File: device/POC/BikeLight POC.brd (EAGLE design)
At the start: 68.6 x 53.3 mm, 3 parts

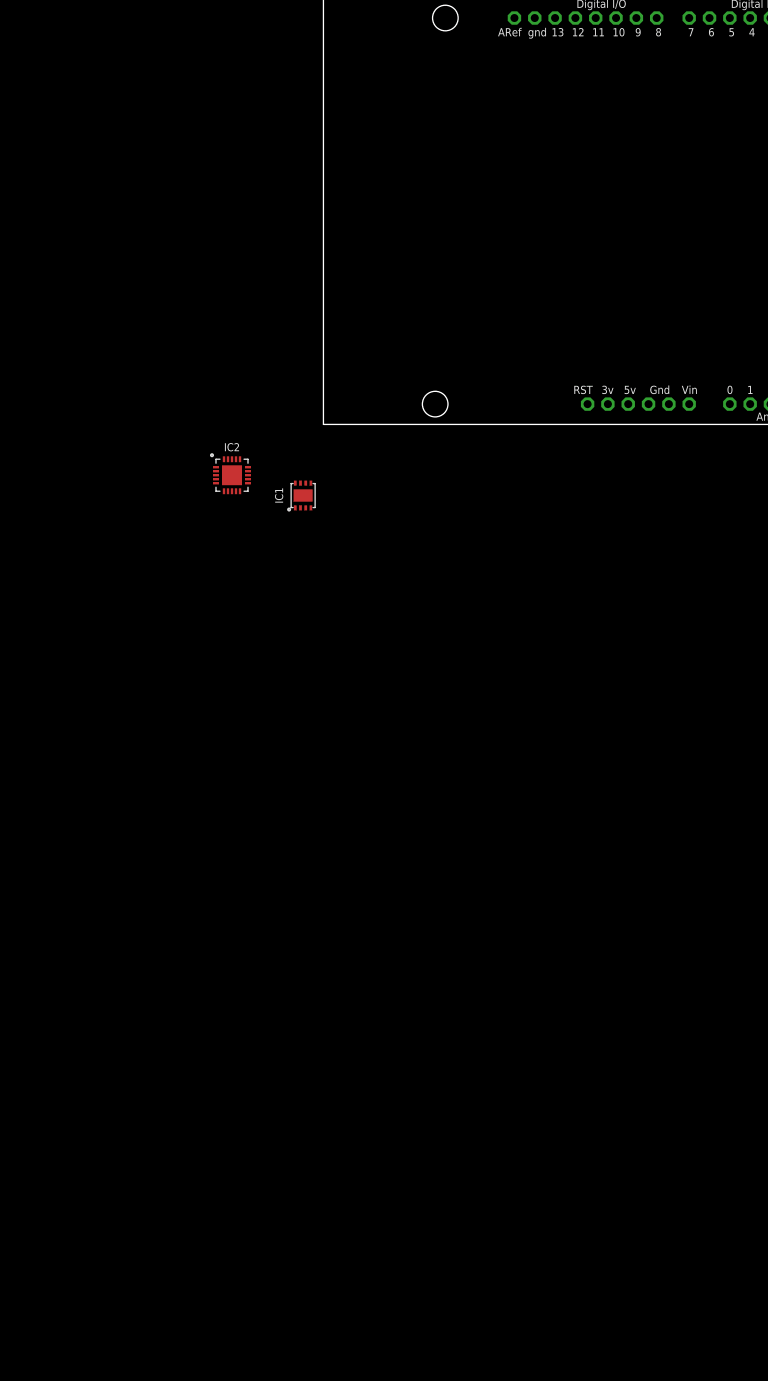
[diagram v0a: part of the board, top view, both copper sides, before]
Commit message: - added SD card with level shifter, FRAM module
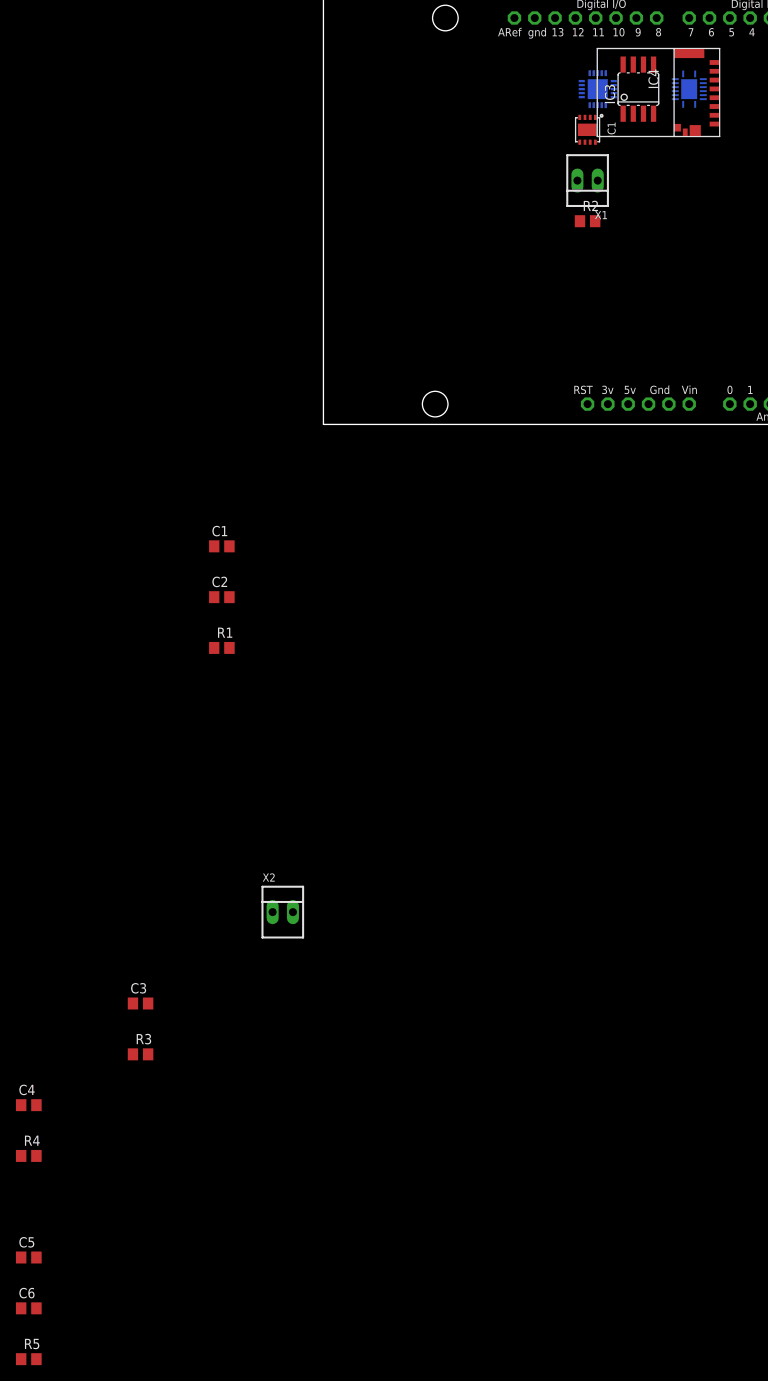
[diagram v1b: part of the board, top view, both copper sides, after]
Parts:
- added C1, C2, C3, C4, C5, C6: 0.1μF, rcl:C0805
- added IC3: FM25W256-SOIC, FM25W256 FERAM:SOIC08
- added IC4: MICROSD_SPI_MODE, Molex SD-47309 SD Card Slot:MICRO_SD_CONNECTOR
- added IC5: (no value), TXB0106 - Logic Level Translator:VQFN16
- added R1, R3, R4, R5: 10k, rcl:R0805
- added R2: 120, rcl:R0805
- added X1, X2: 22-23-2021, con-molex:22-23-2021
- moved IC2 66.5 mm to (34.3, 41.9), flipped to the bottom, turned to 180 degrees
- moved IC1 57.9 mm to (33.0, 36.8), turned to 180 degrees
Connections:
- removed net N$4: IC2.SI
- removed net N$5: IC2.SCK
- removed net N$6: IC2.!CS!
- removed net N$8: IC2.TXCAN
- removed net N$9: IC2.RXCAN
- removed net SPI_SS: U$1.D10
- removed net VCC: IC1.VDD
- removed net VDD: IC2.VDD
- new net 3V3: C4.1, C5.1, IC4.VDD, IC5.VCCA, R4.2
- new net 5V0: C1.1, C2.1, C3.1, C6.1, IC1.VDD, IC2.VDD, IC3.!HOLD!, IC3.!WP!, IC3.VCC, IC5.VCCB, R1.1, R3.2
- new net CANH: IC1.CANH, R2.2, X1.1
- new net CANL: IC1.CANL, R2.1, X1.2
- new net OE: IC5.OE, R5.2, U$1.D7
- new net RXCAN: IC1.RXD, IC2.RXCAN
- new net SD_CARD_DETECT: IC5.B6, U$1.D6
- new net SD_CARD_DETECT_3V3: IC4.DET, IC5.A6
- new net SPI_MISO_3V3: IC4.DAT0, IC5.A2
- new net SPI_MOSI_3V3: IC4.CMD, IC5.A4
- new net SPI_SCK_3V3: IC4.CLK, IC5.A3
- new net SPI_SS_FRAM: IC3.!CS!, R3.1, U$1.D9
- new net SPI_SS_MCP2515: IC2.!CS!, R1.2, U$1.D10
- new net SPI_SS_SD-CARD: IC5.B5, U$1.D8
- new net SPI_SS_SD-CARD_3V3: IC4.CD/DAT3, IC5.A5, R4.1
- new net STBY: IC1.STBY, U$1.D5
- new net TXCAN: IC1.TXD, IC2.TXCAN
- net GND: now also C1.2, C2.2, C3.2, C4.2, C5.2, C6.2, IC3.GND, IC4.GND2, IC4.GND4, IC4.POL, IC4.VSS, IC5.GND, IC5.GND1, R5.1
- net N$3: now also IC2.OSC1; no longer IC2.SO
- net SPI_MISO: now also IC2.SO, IC3.SO, IC5.B2
- net SPI_MOSI: now also IC2.SI, IC3.SI, IC5.B4
- net SPI_SCK: now also IC2.SCK, IC3.SCK, IC5.B3

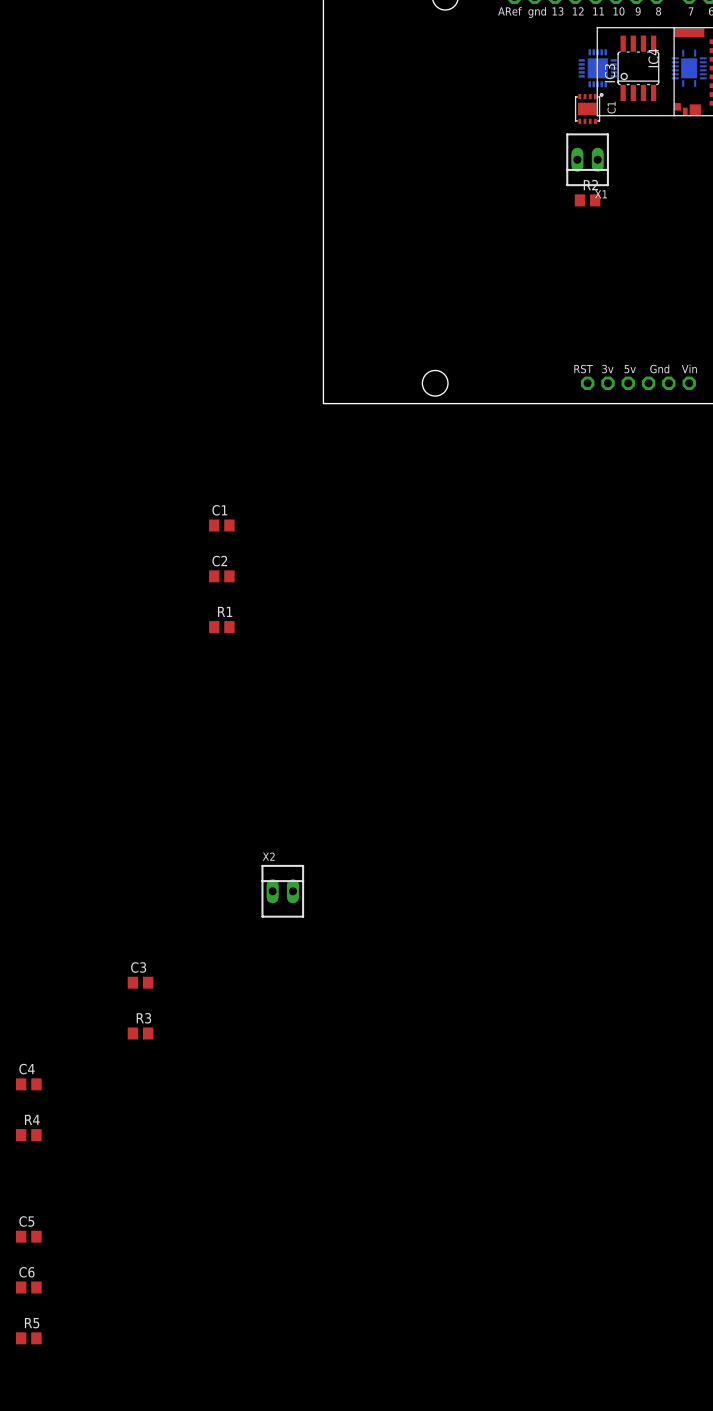
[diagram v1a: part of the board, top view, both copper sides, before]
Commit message: - added few passives to SD card, FRAM, logic level shifter, can hardware
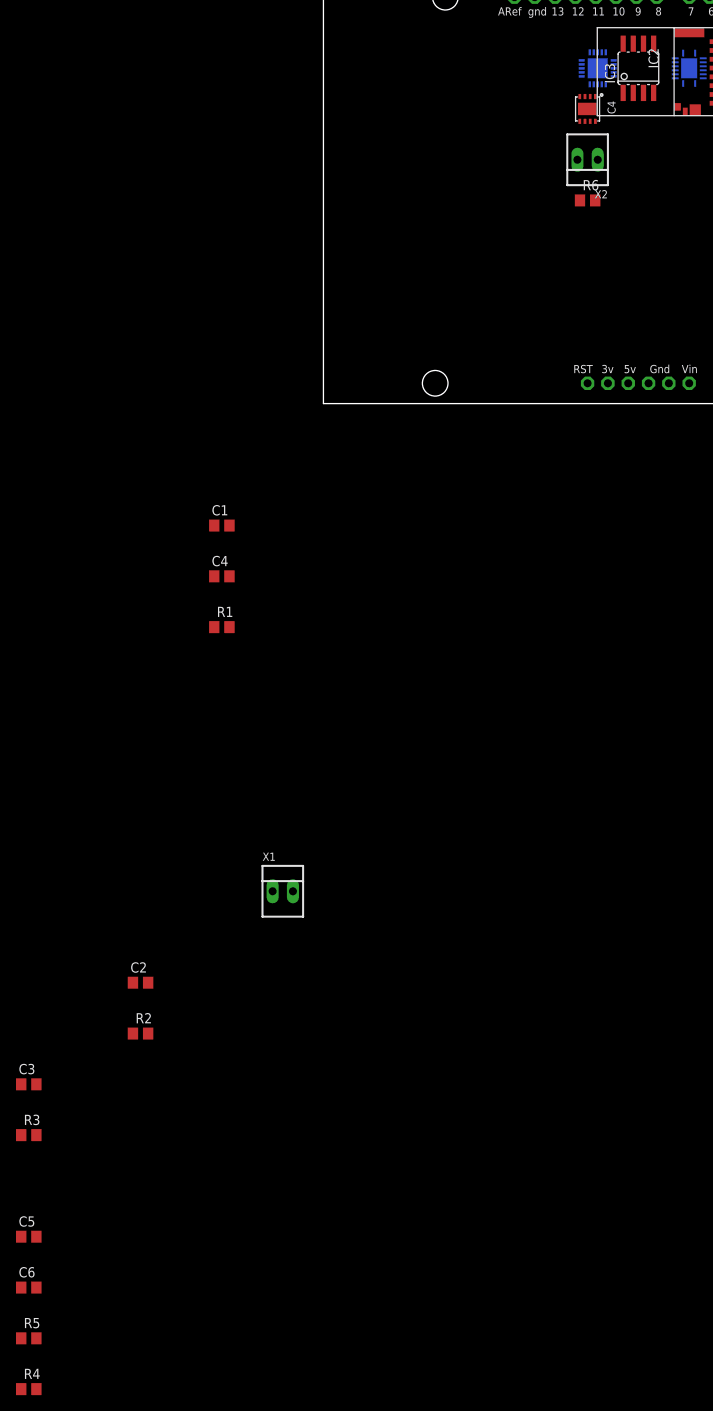
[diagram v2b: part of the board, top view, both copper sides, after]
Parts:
- added R6: 120, rcl:R0805
- BRD1: value ARDUINOUNO -> (none)
- IC1: device MCP2561-2 - High-Speed CAN Transceiver:DFN10 -> MCP2515-I-ML - Standalonce CAN Controller with SPI Interface:QFN20
- IC2: value (none) -> MICROSD_SPI_MODE; device MCP2515-I-ML - Standalonce CAN Controller with SPI Interface:QFN20 -> Molex SD-47309 SD Card Slot:MICRO_SD_CONNECTOR
- IC4: value MICROSD_SPI_MODE -> (none); device Molex SD-47309 SD Card Slot:MICRO_SD_CONNECTOR -> MCP2561-2 - High-Speed CAN Transceiver:DFN10
- R2: value 120 -> 10k
- moved R2 118.2 mm to (-22.9, -78.7)
- moved X1 99.1 mm to (-5.08, -61.0), turned to 0 degrees
- moved X2 99.1 mm to (33.0, 30.5), turned to 180 degrees
- moved C4 67.9 mm to (-12.7, -21.6)
- moved C2 51.8 mm to (-22.9, -72.4)
- moved R4 31.8 mm to (-36.8, -123.2)
- moved IC4 19.4 mm to (33.0, 36.8), turned to 180 degrees
- moved C3 18.9 mm to (-36.8, -85.1)
- moved R3 18.9 mm to (-36.8, -91.4)
- moved IC2 16.1 mm to (49.5, 47.0), flipped to the top, turned to 270 degrees
- moved IC1 5.24 mm to (34.3, 41.9), flipped to the bottom
- renumbered U$1 to BRD1
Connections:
- net 3V3: now also C3.1, IC2.VDD, R3.2; no longer C4.1, IC4.VDD, R4.2
- net 5V0: now also C4.1, IC4.VDD, R2.2, R4.1; no longer C3.1, IC2.VDD, R3.2
- net CANH: now also IC4.CANH, R6.2, X2.1; no longer IC1.CANH, R2.2, X1.1
- net CANL: now also IC4.CANL, R6.1, X2.2; no longer IC1.CANL, R2.1, X1.2
- net GND: now also IC1.GND1, IC1.GND6, IC2.GND2, IC2.GND4, IC2.POL, IC2.VSS, IC4.GND; no longer IC1.VSS, IC2.GND, IC2.GND1, IC2.GND6, IC4.GND2, IC4.GND4, IC4.POL
- net N$3: now also IC1.OSC1; no longer IC2.OSC1
- net N$7: now also IC1.!INT!; no longer IC2.!INT!
- net RXCAN: now also IC1.RXCAN, IC4.RXD; no longer IC1.RXD, IC2.RXCAN
- net SD_CARD_DETECT_3V3: now also IC2.DET; no longer IC4.DET
- net SPI_MISO: now also IC1.SO; no longer IC2.SO
- net SPI_MISO_3V3: now also IC2.DAT0; no longer IC4.DAT0
- net SPI_MOSI: now also IC1.SI; no longer IC2.SI
- net SPI_MOSI_3V3: now also IC2.CMD; no longer IC4.CMD
- net SPI_SCK: now also IC1.SCK; no longer IC2.SCK
- net SPI_SCK_3V3: now also IC2.CLK; no longer IC4.CLK
- net SPI_SS_FRAM: now also R2.1; no longer R3.1
- net SPI_SS_MCP2515: now also IC1.!CS!; no longer IC2.!CS!
- net SPI_SS_SD-CARD_3V3: now also IC2.CD/DAT3, R3.1; no longer IC4.CD/DAT3, R4.1
- net STBY: now also IC4.STBY, R4.2; no longer IC1.STBY
- net TXCAN: now also IC1.TXCAN, IC4.TXD; no longer IC1.TXD, IC2.TXCAN

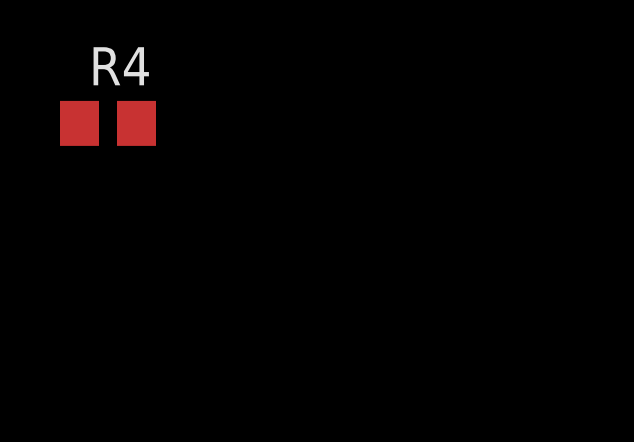
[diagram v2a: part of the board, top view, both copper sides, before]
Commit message: - added 8mhz oscillator to mcp2515
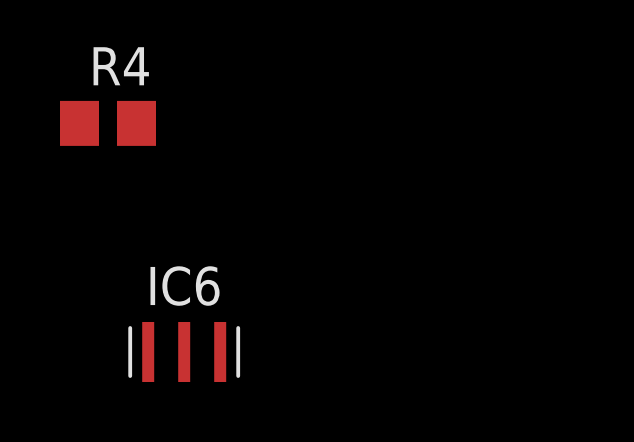
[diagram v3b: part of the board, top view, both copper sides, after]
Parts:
- added IC6: (no value), PRQV8.00CR1510Y00L - 8MHz resonator:SMT
- BRD1: value (none) -> BikeLight POC
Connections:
- removed net 3V: BRD1.3V
- removed net N$2: BRD1.5V
- removed net N$3: IC1.OSC1
- new net OSC1: IC1.OSC1, IC6.XTAL1
- new net OSC2: IC1.OSC2, IC6.XTAL2
- net 3V3: now also BRD1.3V
- net 5V0: now also BRD1.5V
- net GND: now also IC6.GND
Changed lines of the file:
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@@
 </autorouter>
 <elements>
-<element name="BRD1" library="adafruit" library_urn="urn:adsk.eagle:library:420" package="ARDUINO" value="" x="0" y="0"/>
+<element name="BRD1" library="adafruit" library_urn="urn:adsk.eagle:library:420" package="ARDUINO" value="BikeLight POC" x="0" y="0"/>
 <element name="IC4" library="MCP2561-2 - High-Speed CAN Transceiver" package="DFN10" value="" x="33.02" y="36.83" rot="R180"/>
 <element name="IC1" library="MCP2515-I-ML - Standalonce CAN Controller with SPI Interface" package="QFN20" value="" x="34.29" y="41.91" rot="MR180"/>
@@
 <element name="R5" library="rcl" library_urn="urn:adsk.eagle:library:334" package="R0805" package3d_urn="urn:adsk.eagle:package:23553/2" value="10k" x="-36.83" y="-116.84"/>
 <element name="R4" library="rcl" library_urn="urn:adsk.eagle:library:334" package="R0805" package3d_urn="urn:adsk.eagle:package:23553/2" value="10k" x="-36.83" y="-123.19"/>
+<element name="IC6" library="PRQV8.00CR1510Y00L - 8MHz resonator" package="SMT" value="" x="-34.29" y="-130.81"/>
 </elements>
 <signals>
@@
 <contactref element="BRD1" pad="VIN"/>
 </signal>
-<signal name="3V">
-<contactref element="BRD1" pad="3V"/>
-</signal>
 <signal name="N$1">
 <contactref element="BRD1" pad="RESET"/>
-</signal>
-<signal name="N$2">
-<contactref element="BRD1" pad="5V"/>
 </signal>
 <signal name="GND">
@@
 <contactref element="C6" pad="2"/>
 <contactref element="R5" pad="1"/>
+<contactref element="IC6" pad="GND"/>
+<wire x1="-37.78" y1="-116.84" x2="-34.29" y2="-130.81" width="0" layer="19" extent="1-1"/>
 <wire x1="-35.88" y1="-110.49" x2="-37.78" y2="-116.84" width="0" layer="19" extent="1-1"/>
 <wire x1="-35.88" y1="-104.14" x2="-35.88" y2="-110.49" width="0" layer="19" extent="1-1"/>
@@
 <contactref element="C6" pad="1"/>
 <contactref element="R4" pad="1"/>
+<contactref element="BRD1" pad="5V"/>
 <wire x1="-37.78" y1="-110.49" x2="-37.78" y2="-123.19" width="0" layer="19" extent="1-1"/>
 <wire x1="-21.91" y1="-78.74" x2="-37.78" y2="-110.49" width="0" layer="19" extent="1-1"/>
@@
 <wire x1="-13.65" y1="-21.59" x2="-13.65" y2="-27.94" width="0" layer="19" extent="1-1"/>
 <wire x1="-13.65" y1="-15.24" x2="-13.65" y2="-21.59" width="0" layer="19" extent="1-1"/>
-<wire x1="32.695" y1="38.38" x2="-13.65" y2="-15.24" width="0" layer="19" extent="1-1"/>
+<wire x1="38.1" y1="2.54" x2="-13.65" y2="-15.24" width="0" layer="19" extent="1-1"/>
+<wire x1="32.695" y1="38.38" x2="38.1" y2="2.54" width="0" layer="19" extent="1-1"/>
 <wire x1="34.29" y1="39.91" x2="32.695" y2="38.38" width="0" layer="19" extent="1-16"/>
 <wire x1="40.005" y1="38.8366" x2="34.29" y2="39.91" width="0" layer="19" extent="1-16"/>
@@
 <wire x1="50.8" y1="50.8" x2="33.995" y2="35.28" width="0" layer="19" extent="1-1"/>
 </signal>
-<signal name="N$3">
+<signal name="OSC1">
 <contactref element="IC1" pad="OSC1"/>
+<contactref element="IC6" pad="XTAL1"/>
+<wire x1="33.79" y1="43.91" x2="-35.49" y2="-130.81" width="0" layer="19" extent="1-16"/>
 </signal>
 <signal name="SPI_SS_FRAM">
@@
 <contactref element="IC5" pad="VCCA"/>
 <contactref element="C5" pad="1"/>
+<contactref element="BRD1" pad="3V"/>
 <wire x1="-35.88" y1="-91.44" x2="-37.78" y2="-104.14" width="0" layer="19" extent="1-1"/>
 <wire x1="-37.78" y1="-85.09" x2="-35.88" y2="-91.44" width="0" layer="19" extent="1-1"/>
-<wire x1="48.9" y1="40.84" x2="-37.78" y2="-85.09" width="0" layer="19" extent="1-1"/>
+<wire x1="35.56" y1="2.54" x2="-37.78" y2="-85.09" width="0" layer="19" extent="1-1"/>
+<wire x1="48.9" y1="40.84" x2="35.56" y2="2.54" width="0" layer="19" extent="1-1"/>
 <wire x1="47.47" y1="43.16" x2="48.9" y2="40.84" width="0" layer="19" extent="1-16"/>
 </signal>
@@
 <wire x1="45.72" y1="50.8" x2="46.47" y2="40.01" width="0" layer="19" extent="16-16"/>
 </signal>
+<signal name="OSC2">
+<contactref element="IC1" pad="OSC2"/>
+<contactref element="IC6" pad="XTAL2"/>
+<wire x1="33.29" y1="43.91" x2="-33.09" y2="-130.81" width="0" layer="19" extent="1-16"/>
+</signal>
 </signals>

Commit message: - added MCP1802 LDO.lbr and datasheet - incorporated LDOs (3V3 and 5V0) into schematic - redeployed brd from scratch
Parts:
- added C10, C11, C8, C9: 4.7μF, rcl:C0805
- added C7: 0.1μF, rcl:C0805
- added IC10: MCP1802T-5002I/OT, MCP1802 LDO:SOT23-5
- added IC7: ADXL345, ADXL345 Accelerometer:LGA14
- added IC8: 74HCT1G32, 74HCT1G32GW - OR Gate:SOT353/5
- added IC9: MCP1802T-3302I/OT, MCP1802 LDO:SOT23-5
- added R7: 10k, rcl:R0805
- added R8: 100k, rcl:R0805
- added S1: SWS001, smd-special:SMS-001
- IC1: value (none) -> MCP2515-I-ML
- IC4: value (none) -> MCP2561-2
- IC5: value (none) -> TXB0106
- IC6: value (none) -> PRQV8.00CR1510Y00L
- moved R4 210.5 mm to (-67.3, 85.1)
- moved IC6 207.0 mm to (-38.1, 76.2)
- moved R5 205.0 mm to (-72.4, 85.1)
- moved C6 194.2 mm to (-90.2, 76.2)
- moved C5 186.4 mm to (-83.8, 76.2)
- moved R3 178.3 mm to (-62.2, 85.1)
- moved R2 167.4 mm to (-57.1, 85.1)
- moved C3 164.9 mm to (-71.1, 76.2)
- moved C2 154.4 mm to (-64.8, 76.2)
- moved X1 137.5 mm to (-68.6, 61.0)
- moved IC1 122.0 mm to (-86.4, 59.7), flipped to the top, turned to 0 degrees
- moved R1 119.7 mm to (-52.1, 85.1)
- moved C4 117.3 mm to (-77.5, 76.2)
- moved X2 114.6 mm to (-77.5, 61.0), turned to 0 degrees
- moved C1 102.2 mm to (-58.4, 76.2)
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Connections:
- net SPI_SS_FRAM renamed P0.23-SPI_SS_FRAM
- net SPI_SS_MCP2515 renamed P0.24-SPI_SS_MCP2515
- net SPI_SS_SD-CARD renamed P0.20-SPI_SS_SD-CARD
- removed net N$7: IC1.!INT!
- removed net OE: BRD1.D7, IC5.OE, R5.2
- removed net SD_CARD_DETECT: BRD1.D6, IC5.B6
- removed net SPI_MISO: BRD1.D12, IC1.SO, IC3.SO, IC5.B2
- removed net SPI_MOSI: BRD1.D11, IC1.SI, IC3.SI, IC5.B4
- removed net SPI_SCK: BRD1.D13, IC1.SCK, IC3.SCK, IC5.B3
- removed net STBY: BRD1.D5, IC4.STBY, R4.2
- new net !SNDN!: IC10.!SHDN!, IC9.!SHDN!, R8.2, S1.1
- new net P0.00-: BRD1.AREF
- new net P0.01-VLIION: BRD1.A0, C10.1, C8.1, IC10.VIN, IC9.VIN, S1.2, X1.1
- new net P0.02-: BRD1.A1
- new net P0.03-: BRD1.A2
- new net P0.04-: BRD1.A3
- new net P0.05-: BRD1.A4
- new net P0.06-: BRD1.A5
- new net P0.12-: BRD1.D0
- new net P0.13-ADXL345_INT1_INTERRUPT_PIN: BRD1.D1, IC7.INT1
- new net P0.14-: BRD1.D2
- new net P0.15-MCP2515_INT: BRD1.D3, IC1.!INT!
- new net P0.16-STBY: BRD1.D4, IC4.STBY, R4.2
- new net P0.17-SD_CARD_DETECT: BRD1.D5, IC5.B6
- new net P0.18-OE: BRD1.D6, IC5.OE, R5.2
- new net P0.19-SPI_SS_ADXL345_PIN: BRD1.D7, IC7.!CS!, IC8.A, R7.2
- new net P0.25-SPI_MOSI: BRD1.D11, IC1.SI, IC3.SI, IC5.B4, IC8.B
- new net P0.28-SPI_MISO: BRD1.D12, IC1.SO, IC3.SO, IC5.B2, IC7.SDO
- new net P0.29-SPI_SCK: BRD1.D13, IC1.SCK, IC3.SCK, IC5.B3, IC7.SCL
- new net SDA: IC7.SDA, IC8.Y
- net 3V3: now also C9.1, IC9.VOUT
- net 5V0: now also C11.1, C7.2, IC10.VOUT, IC7.VCC, IC7.VDD, IC8.VCC, R7.1
- net GND: now also C10.2, C11.2, C7.1, C8.2, C9.2, IC10.GND, IC7.GND1, IC7.GND2, IC7.GND3, IC8.GND, IC9.GND, R8.1, X1.2
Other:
- board size 68.6 x 53.3 mm -> 160 x 100 mm

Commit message: - finished schematic, ERC is checked and reports only known approved issues
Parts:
- moved IC8 86.4 mm to (-96.5, 0.00)
- moved BRD1 81.3 mm to (0.00, 0.00)
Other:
- board size 160 x 100 mm -> 68.6 x 53.3 mm
